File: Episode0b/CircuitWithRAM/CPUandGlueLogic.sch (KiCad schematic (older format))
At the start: 27 parts, among them SW100 SW_Push, U100 74HCT245, U101 74HCT245, U102 MAX708, U103 HD6809, U104 74HCT245, U105 74HCT365, U106 74HCT00, U107 74HCT27, U108 74HCT138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

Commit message: connected a couple unconnected inputs
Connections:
- wire segments 321 -> 324
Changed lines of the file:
@@
 Wire Wire Line
 	4150 1850 3450 1850
+Connection ~ 3450 1850
+Text HLabel 10350 2600 2    50   Output ~ 0
+~ROMEN~
+Text HLabel 10350 2200 2    50   Output ~ 0
+~RAMEN~
+Wire Wire Line
+	6050 6350 6400 6350
+Wire Wire Line
+	6400 6350 6400 6300
+$Comp
+L power:VCC #PWR?
+U 1 1 5DC2F3B1
+P 6400 6300
+F 0 "#PWR?" H 6400 6150 50  0001 C CNN
+F 1 "VCC" H 6417 6473 50  0000 C CNN
+F 2 "" H 6400 6300 50  0001 C CNN
+F 3 "" H 6400 6300 50  0001 C CNN
+	1    6400 6300
+	1    0    0    -1
+$EndComp
+Wire Wire Line
+	5250 7150 5250 7250
 Wire Bus Line
 	1000 5700 3650 5700
@@
 Wire Bus Line
 	2450 6150 2450 9200
-Connection ~ 3450 1850
-Text HLabel 10350 2600 2    50   Output ~ 0
-~ROMEN~
-Text HLabel 10350 2200 2    50   Output ~ 0
-~RAMEN~
+$Comp
+L power:GND #PWR?
+U 1 1 5DC72C2F
+P 5250 7250
+F 0 "#PWR?" H 5250 7000 50  0001 C CNN
+F 1 "GND" H 5255 7077 50  0000 C CNN
+F 2 "" H 5250 7250 50  0001 C CNN
+F 3 "" H 5250 7250 50  0001 C CNN
+	1    5250 7250
+	1    0    0    -1
+$EndComp
 $EndSCHEMATC

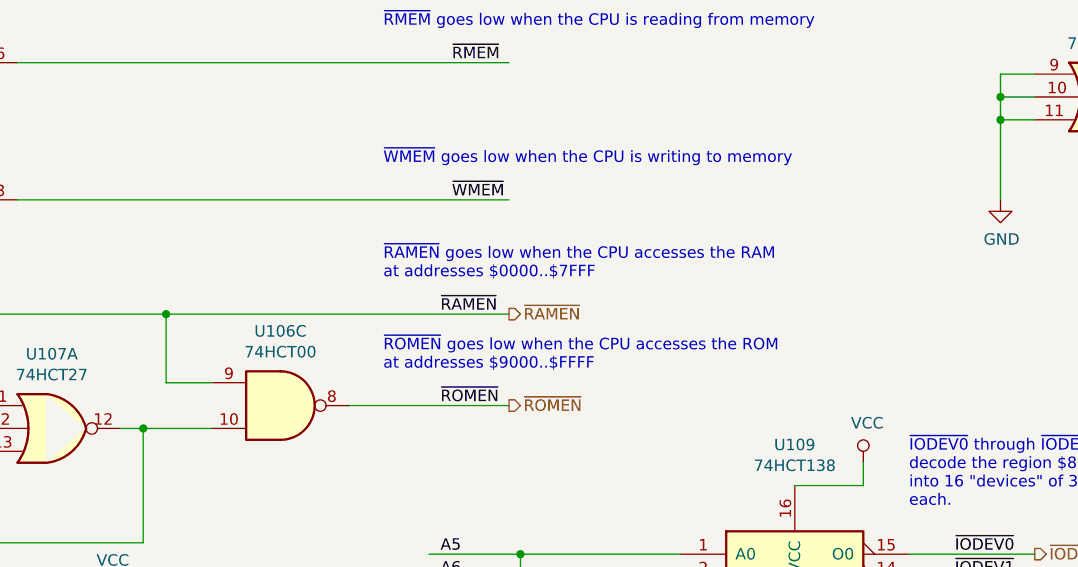
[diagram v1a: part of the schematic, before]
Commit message: just use (buffered) A15 as RAM enable
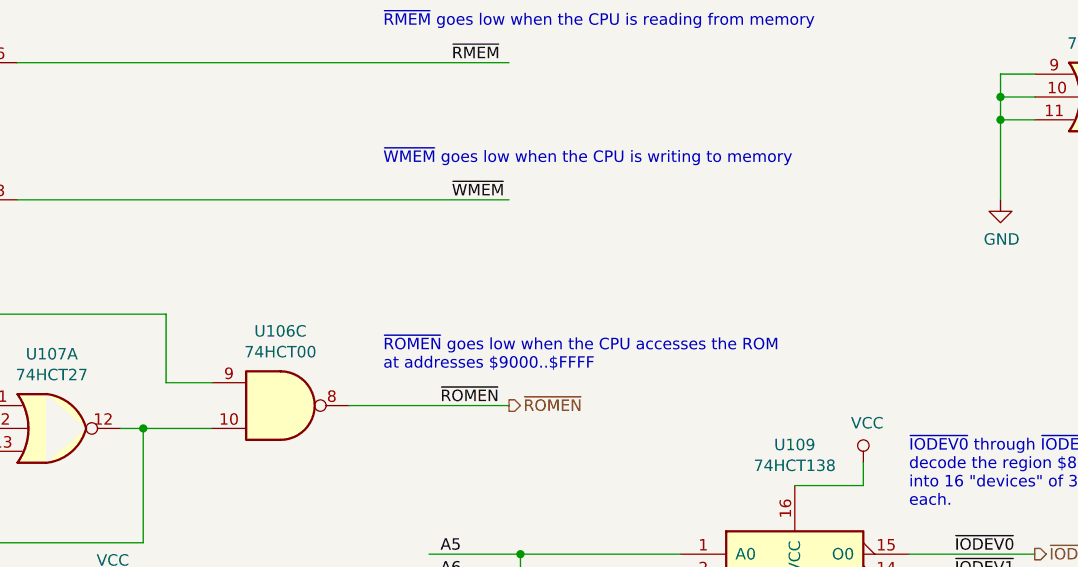
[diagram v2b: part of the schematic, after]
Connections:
- net labels removed: ~RAMEN, ~RAMEN~
- wire segments 324 -> 323
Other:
- note removed: "~RAMEN~ goes low when the CPU accesses the RAM\nat addresses $0000..$7FFF"
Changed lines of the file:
@@
 Text Label 6750 2200 0    50   ~ 0
 A15
-Text Label 10050 2200 0    50   ~ 0
-~RAMEN
 Wire Wire Line
 	9050 2500 8850 2500
 Wire Wire Line
 	8850 2500 8850 2200
-Connection ~ 8850 2200
-Wire Wire Line
-	8850 2200 10350 2200
 Wire Wire Line
 	9650 2600 10350 2600
@@
 Text Notes 9800 1550 0    50   ~ 0
 ~WMEM~ goes low when the CPU is writing to memory
-Text Notes 9800 2050 0    50   ~ 0
-~RAMEN~ goes low when the CPU accesses the RAM\nat addresses $0000..$7FFF
 Text Notes 9800 2450 0    50   ~ 0
 ~ROMEN~ goes low when the CPU accesses the ROM\nat addresses $9000..$FFFF
@@
 Text HLabel 10350 2600 2    50   Output ~ 0
 ~ROMEN~
-Text HLabel 10350 2200 2    50   Output ~ 0
-~RAMEN~
 Wire Wire Line
 	6050 6350 6400 6350
@@
 Wire Wire Line
 	5250 7150 5250 7250
+$Comp
+L power:GND #PWR?
+U 1 1 5DC72C2F
+P 5250 7250
+F 0 "#PWR?" H 5250 7000 50  0001 C CNN
+F 1 "GND" H 5255 7077 50  0000 C CNN
+F 2 "" H 5250 7250 50  0001 C CNN
+F 3 "" H 5250 7250 50  0001 C CNN
+	1    5250 7250
+	1    0    0    -1
+$EndComp
 Wire Bus Line
 	1000 5700 3650 5700
@@
 Wire Bus Line
 	2450 6150 2450 9200
-$Comp
-L power:GND #PWR?
-U 1 1 5DC72C2F
-P 5250 7250
-F 0 "#PWR?" H 5250 7000 50  0001 C CNN
-F 1 "GND" H 5255 7077 50  0000 C CNN
-F 2 "" H 5250 7250 50  0001 C CNN
-F 3 "" H 5250 7250 50  0001 C CNN
-	1    5250 7250
-	1    0    0    -1
-$EndComp
 $EndSCHEMATC
